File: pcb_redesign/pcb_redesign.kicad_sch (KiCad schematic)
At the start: 7 parts, among them U1 ESP32-S3-WROOM-1

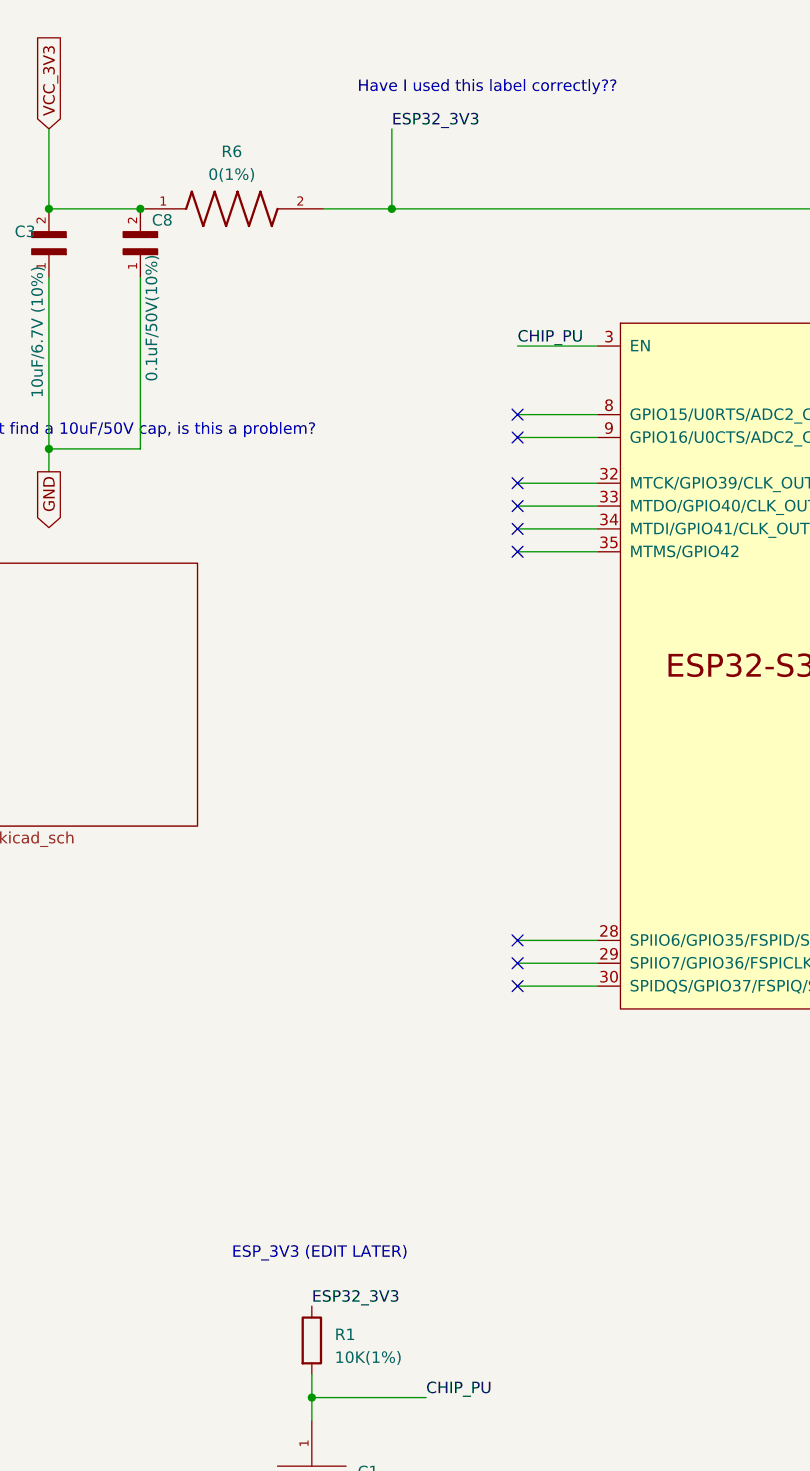
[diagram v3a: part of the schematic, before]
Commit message: wired up 2.13
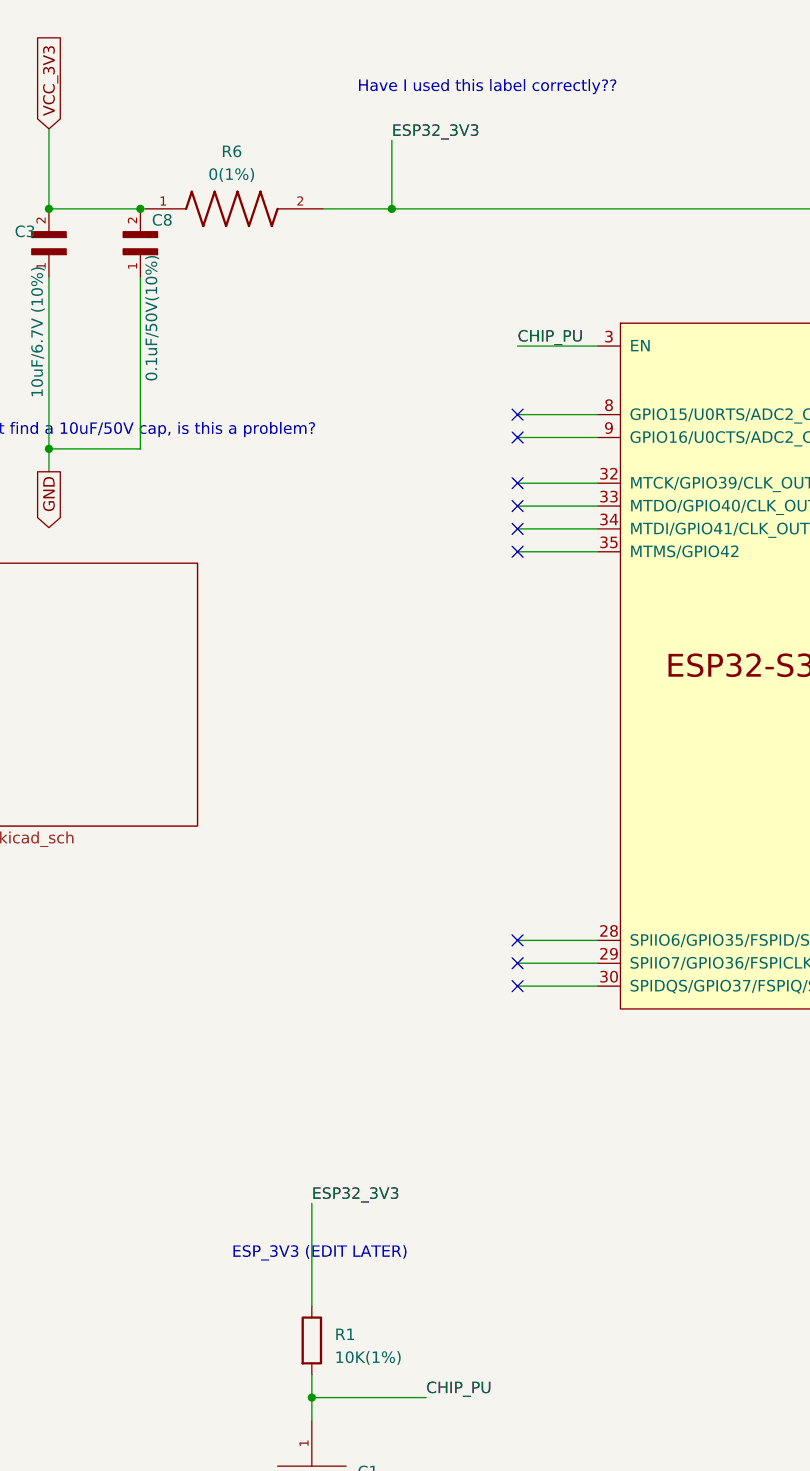
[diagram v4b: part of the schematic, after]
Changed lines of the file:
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@@
     (stroke (width 0) (type default))
   )
-  (wire (pts (xy 74.93 34.29) (xy 74.93 43.18))
+  (wire (pts (xy 74.93 35.56) (xy 74.93 43.18))
     (stroke (width 0) (type default))
   )
@@
   )
   (wire (pts (xy 189.23 78.74) (xy 199.39 78.74))
+    (stroke (width 0) (type default))
+  )
+  (wire (pts (xy 66.04 153.67) (xy 66.04 165.1))
     (stroke (width 0) (type default))
   )
@@
     (effects (font (size 1.27 1.27)) (justify left bottom))
   )
-  (label "ESP32_3V3" (at 66.04 165.1 0) (fields_autoplaced)
-    (effects (font (size 1.27 1.27)) (justify left bottom))
-  )
-  (label "ESP32_3V3" (at 74.93 34.29 0) (fields_autoplaced)
-    (effects (font (size 1.27 1.27)) (justify left bottom))
-  )
+  (label "ESP32_3V3" (at 66.04 153.67 0) (fields_autoplaced)
+    (effects (font (size 1.27 1.27)) (justify left bottom))
+  )
+  (label "ESP32_3V3" (at 74.93 35.56 0) (fields_autoplaced)
+    (effects (font (size 1.27 1.27)) (justify left bottom))
+  )

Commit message: finished design
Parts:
- C1, C8: footprint 1uF_cap_0603:CL10A105KB8NNNC -> Capacitor_SMD:C_0603_1608Metric
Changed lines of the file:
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@@
       (effects (font (size 1.27 1.27)) (justify right))
     )
-    (property "Footprint" "1uF_cap_0603:CL10A105KB8NNNC" (at 46.99 48.26 0)
+    (property "Footprint" "Capacitor_SMD:C_0603_1608Metric" (at 46.99 48.26 0)
       (effects (font (size 1.27 1.27)) (justify bottom) hide)
     )
@@
       (effects (font (size 1.27 1.27)) (justify left))
     )
-    (property "Footprint" "1uF_cap_0603:CL10A105KB8NNNC" (at 66.04 184.15 0)
+    (property "Footprint" "Capacitor_SMD:C_0603_1608Metric" (at 66.04 184.15 0)
       (effects (font (size 1.27 1.27)) hide)
     )
